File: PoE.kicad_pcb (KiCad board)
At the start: 4 copper layers, 102.5 x 35 mm, 88 parts, among them J1001 8P8C_LED_Shielded_x2, J1002 8P8C_LED_Shielded_x2, Q2001 FDC86244, U1001 7490220122, U1002 TCMT1107, U2001 TPS23751PWP, U2002 TCMT1107, U2003 TLV431ACDBZR

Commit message: New layout attempt
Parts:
- CR2001: moved to B.Cu
- D1001, D1002, D1006, D1007: moved to F.Cu
- moved C1006 36.8 mm to (70.5, 48.2), turned to 0 degrees
- moved C2002 14.4 mm to (51.6, 45.2), turned to 180 degrees
- moved D1006 12.9 mm to (48.4, 39.0)
- moved D1001 12.8 mm to (57.4, 39.0)
- moved U1002 9.84 mm to (95.2, 25.1)
- moved CR2001 9.65 mm to (56.5, 26.0)
- moved U2002 9.22 mm to (95.2, 28.8)
- moved R2001 6.30 mm to (58.5, 25.0)
- moved R2003 6.30 mm to (54.5, 25.0)
- moved R2002 6.10 mm to (58.5, 27.0)
- moved R2004 6.00 mm to (54.5, 27.0)
- moved C2009 5.90 mm to (67.6, 44.0)
- moved D1008 4.64 mm to (48.4, 32.0)
- moved D1003 4.46 mm to (57.4, 32.0)
- moved D1009 3.11 mm to (48.4, 39.0)
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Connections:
- U2001 pad V: (no net) -> VSS
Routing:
- net T2P: track 0.00 -> 54.0 mm, vias 0 -> 2
- net /Flyback/T_PRI: track 0.00 -> 48.6 mm, vias 0 -> 7
- net /D_IN: track 26.1 -> 69.9 mm, vias 8 -> 7
- net Net-(U2001-SRT): track 2.01 -> 34.8 mm, vias 0 -> 2
- net VSS: track 0.00 -> 26.4 mm, vias 0 -> 2
- net Net-(U2001-CS): track 0.00 -> 24.7 mm, vias 0 -> 2
- net /C_IN: track 32.4 -> 56.4 mm, vias 7 -> 6
- net /VSS_PRIME: track 17.9 -> 41.2 mm, vias 8 -> 3
- net /VDD_PRIME: track 17.9 -> 40.2 mm, vias 0 -> 3
- net Net-(U2001-VB): track 12.8 -> 32.8 mm, vias 0 -> 1
- net /Flyback/VC: track 0.00 -> 17.7 mm, vias 0 -> 2
- net VDD: track 3.23 -> 19.7 mm, vias 1 -> 2
- net /B_IN: track 35.5 -> 48.6 mm, vias 11 -> 7
- net Net-(U2001-CTL): track 5.27 -> 11.8 mm, vias 0 -> 1
- net Net-(U2001-GATE): track 0.00 -> 5.59 mm, vias 0 -> 1
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- removed copper zone on In2.Cu, net /A_IN
- removed copper zone on In1.Cu, net /B_IN
- removed copper zone on In2.Cu, net /B_IN
- removed copper zone on In2.Cu, net /C_IN
- removed copper zone on In1.Cu, net /D_IN
- removed copper zone on F.Cu, net /VDD_PRIME
- removed copper zone on B.Cu, net /VSS_PRIME
- removed copper zone on F.Cu, net /VSS_PRIME

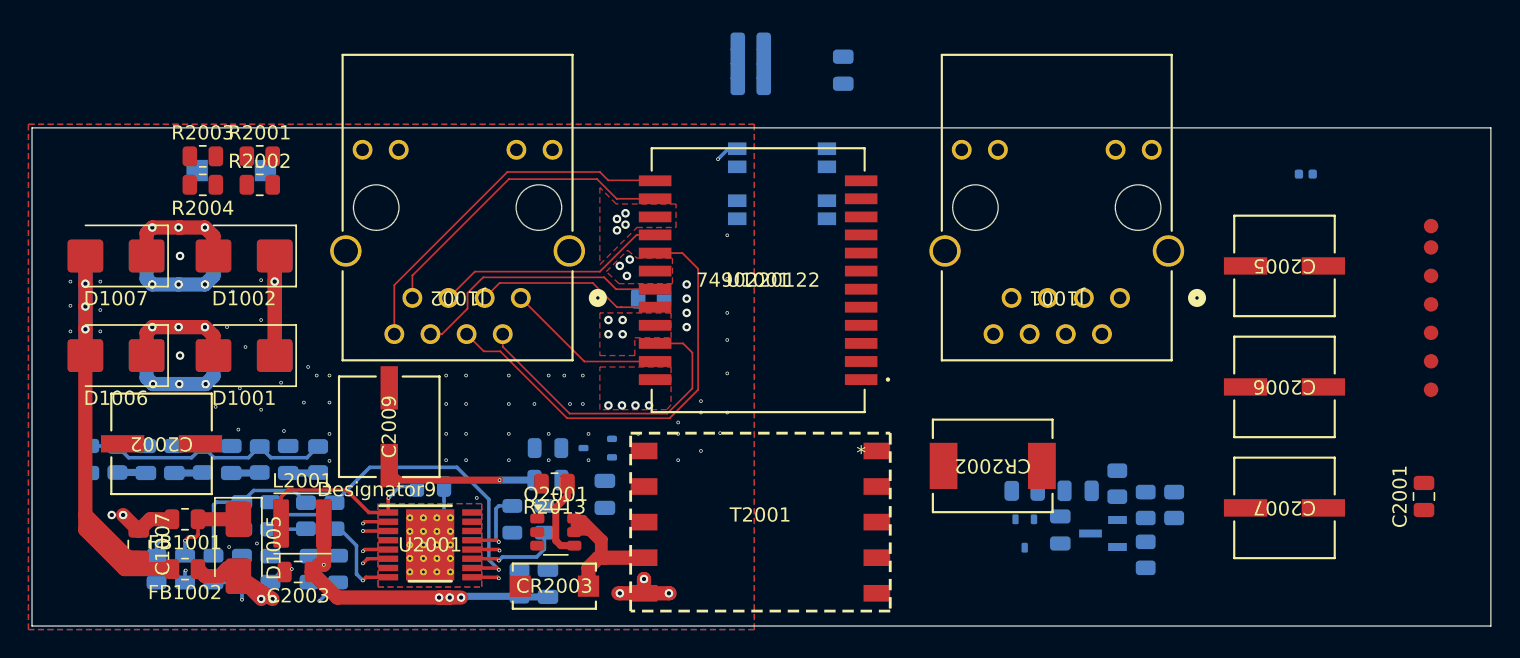
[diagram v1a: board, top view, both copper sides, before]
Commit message: Changed main FET
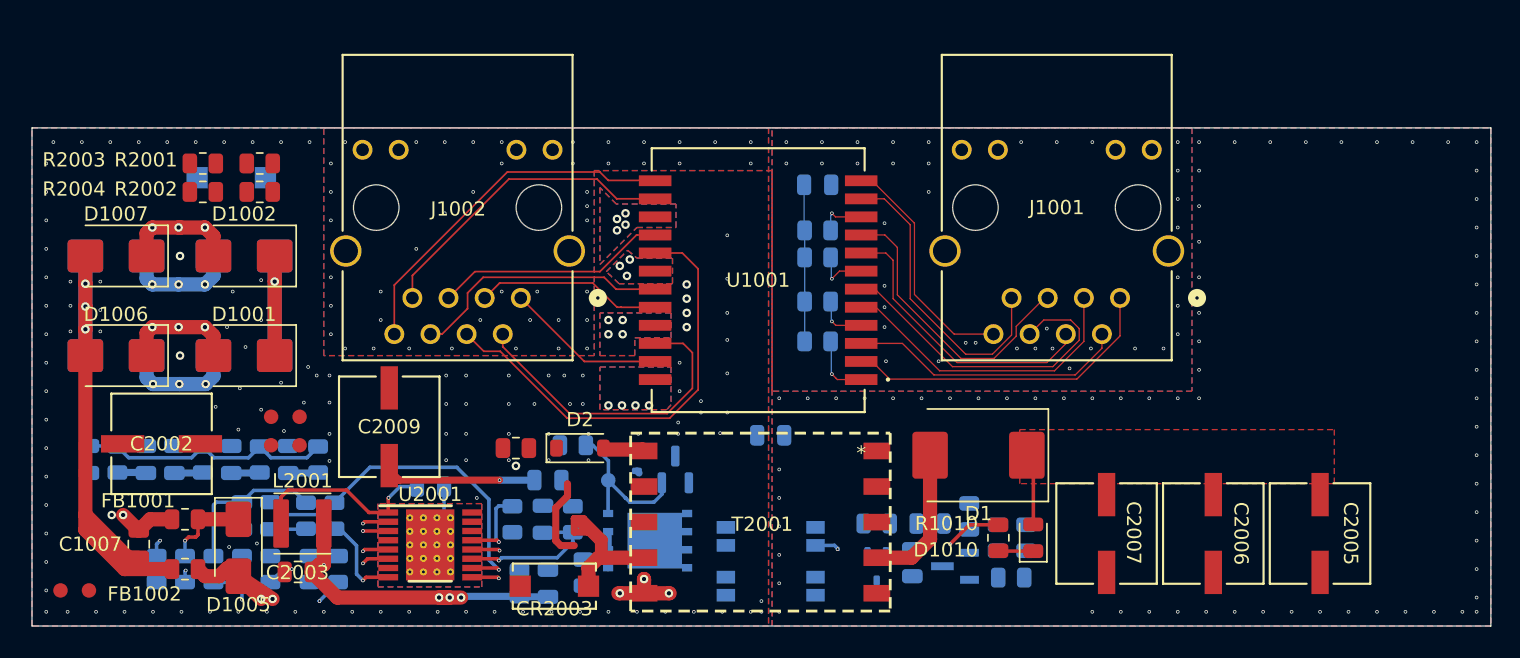
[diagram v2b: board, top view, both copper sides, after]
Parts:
- removed CR2002: MBRS540T3G, footprints:DIODE_SMC_7P15X6P25_ONS
- removed D2001: BAS16W, Package_TO_SOT_SMD:SOT-323_SC-70
- removed Q2001: FDC86244, Package_TO_SOT_SMD:SuperSOT-6
- removed TP1007: TestPoint, SparkFun-Connector:TestPoint-1.0mm
- added D1: B340, Diode_SMD:D_SMC, F.Cu at (109.0, 46.0)
- added D2: 1N4148W, Diode_SMD:D_SOD-123, F.Cu at (81.0, 45.5)
- added D3: BAS16W, Package_TO_SOT_SMD:SOT-323_SC-70, B.Cu at (84.0, 47.8)
- added Q1: SI7898DP-T1-E3, footprints:MOSFET_50DP-T1-E3_VIS, B.Cu at (85.8, 52.0)
- added Q2: MMBT3906, Package_TO_SOT_SMD:SOT-23, B.Cu at (87.7, 47.0)
- added R1: 10k, Resistor_SMD:R_0805_2012Metric, B.Cu at (80.5, 45.3)
- C2001, R2013: moved to B.Cu
- D1010: footprint LED_SMD:LED_0402_1005Metric -> LED_SMD:LED_0805_2012Metric; moved to F.Cu
- R1010: moved to F.Cu
- R2006, R2007, R2009, R2012: footprint LED_SMD:LED_0805_2012Metric -> Resistor_SMD:R_0805_2012Metric
- R2008: value 49.9 -> 10; footprint LED_SMD:LED_0805_2012Metric -> Resistor_SMD:R_0805_2012Metric; moved to F.Cu
- R2010: value 49.9 -> 43.2; footprint LED_SMD:LED_0805_2012Metric -> Resistor_SMD:R_0805_2012Metric
- R2011: value 0 -> 332; footprint LED_SMD:LED_0805_2012Metric -> Resistor_SMD:R_0805_2012Metric
- moved TP1006 99.3 mm to (44.5, 55.5), turned to 0 degrees
- moved TP1001 97.7 mm to (46.5, 55.5), turned to 0 degrees
- moved TP1005 82.1 mm to (59.3, 43.3), turned to 0 degrees
- moved TP1003 81.9 mm to (59.3, 45.3), turned to 0 degrees
- moved TP1002 80.1 mm to (61.3, 45.3), turned to 0 degrees
- moved TP1004 79.5 mm to (61.3, 43.3), turned to 0 degrees
- moved C2001 46.1 mm to (94.4, 44.6), turned to 0 degrees
- moved D1010 31.9 mm to (112.8, 51.8), turned to 90 degrees
- moved R1010 29.6 mm to (110.4, 51.8), turned to 90 degrees
- moved U1002 26.6 mm to (94.4, 51.7)
- moved U2002 26.5 mm to (94.4, 55.2)
- moved R1001 21.5 mm to (97.7, 38.0)
- moved C2005 19.0 mm to (133.0, 51.5), turned to -90 degrees
- moved R1002 17.8 mm to (97.7, 35.2)
- moved R1003 13.9 mm to (97.7, 32.1)
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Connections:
- net Net-(C1002-Pad2) renamed /TEST_A
- net Net-(C1003-Pad2) renamed /TEST_B
- net Net-(C1004-Pad2) renamed /TEST_C
- net Net-(C1005-Pad2) renamed /TEST_D
- C1001 pad 2: unconnected-(C1001-Pad2) -> GNDPWR
- J1001 pad SH: GNDREF -> GNDPWR
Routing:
- net (no net): track 0.00 -> 67.7 mm, vias 0 -> 8
- net Net-(U2001-SRT): track 34.8 -> 0.00 mm, vias 2 -> 0
- net /ETH3: track 0.00 -> 23.3 mm
- net /ETH0: track 0.00 -> 22.6 mm
- net /ETH2: track 0.00 -> 21.4 mm
- net /ETH6: track 0.00 -> 21.3 mm
- net /ETH5: track 0.00 -> 20.8 mm
- net /ETH1: track 0.00 -> 20.6 mm
- net /ETH4: track 0.00 -> 20.4 mm
- net /ETH7: track 0.00 -> 16.7 mm
- net Net-(U2001-CS): track 24.7 -> 10.5 mm, vias 2 -> 1
- net Net-(R1010-Pad2): track 0.00 -> 13.8 mm, vias 0 -> 1
- net Net-(D3-K): track 0.00 -> 11.2 mm
- net Net-(C1001-Pad1): track 0.00 -> 11.1 mm
- net Net-(D1-A): track 0.00 -> 10.2 mm
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- added copper zone on F.Cu, net +5V
- added copper zone on B.Cu, net /A_IN
- added copper zone on In1.Cu, net /A_IN
- added copper zone on In2.Cu, net /A_IN
- added copper zone on B.Cu, net /B_IN
- added copper zone on In1.Cu, net /B_IN
- added copper zone on In2.Cu, net /B_IN
- added copper zone on B.Cu, net /C_IN
- added copper zone on In1.Cu, net /C_IN
- added copper zone on In2.Cu, net /C_IN
- added copper zone on B.Cu, net /D_IN
- added copper zone on In1.Cu, net /D_IN
- added copper zone on In2.Cu, net /D_IN
- added copper zone on B.Cu, net GNDPWR
- added copper zone on F.Cu, net GNDPWR
- added copper zone on In1.Cu, net GNDPWR
- added copper zone on In2.Cu, net GNDPWR
- added copper zone on B.Cu, net GNDREF
- added copper zone on F.Cu, net GNDREF
- added copper zone on In1.Cu, net GNDREF
- added copper zone on In2.Cu, net GNDREF

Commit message: More routing
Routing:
- net T2P: track 52.4 -> 30.8 mm, vias 1 -> 2
- net /B_IN: track 48.6 -> 66.4 mm, vias 7 -> 8
- net /C_IN: track 56.4 -> 71.8 mm
- net /A_IN: track 43.3 -> 54.5 mm
- net /D_IN: track 69.9 -> 75.8 mm
- net GND: vias 124 -> 113

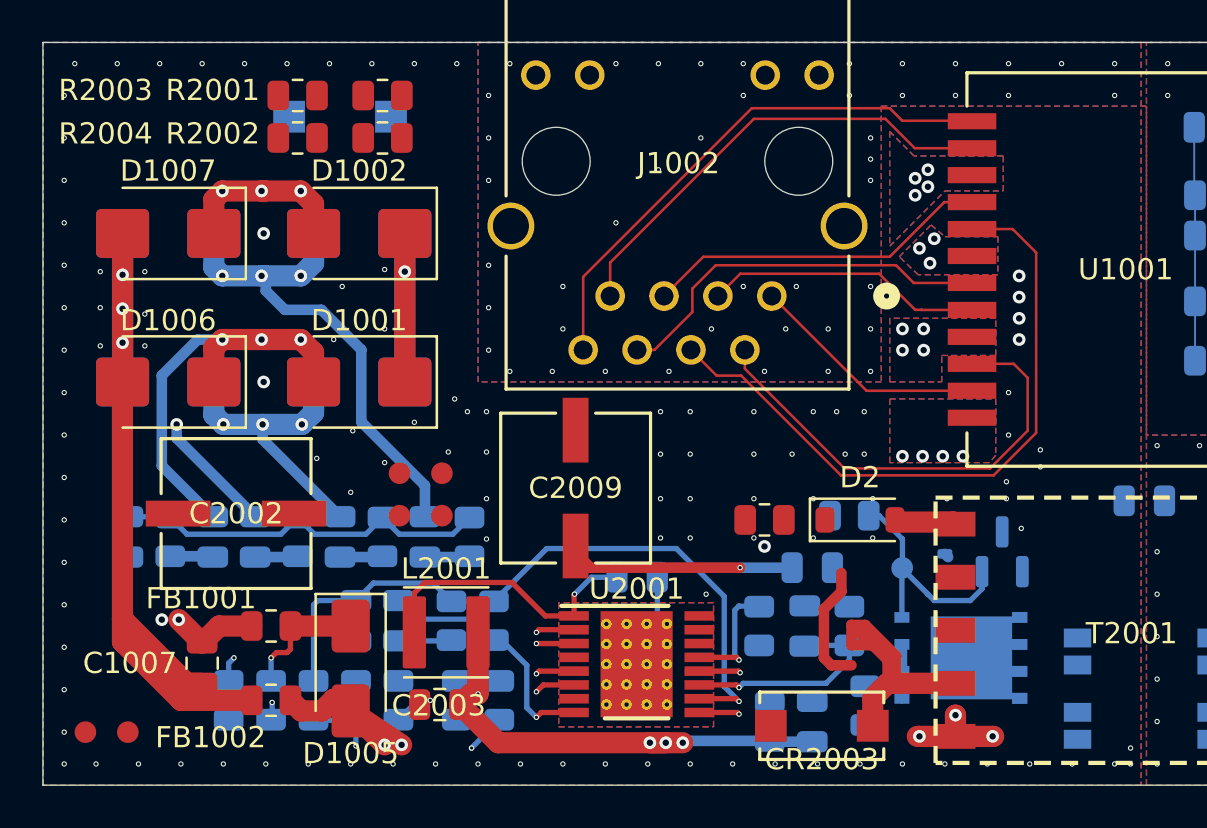
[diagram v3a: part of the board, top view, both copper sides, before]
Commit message: Added more routing
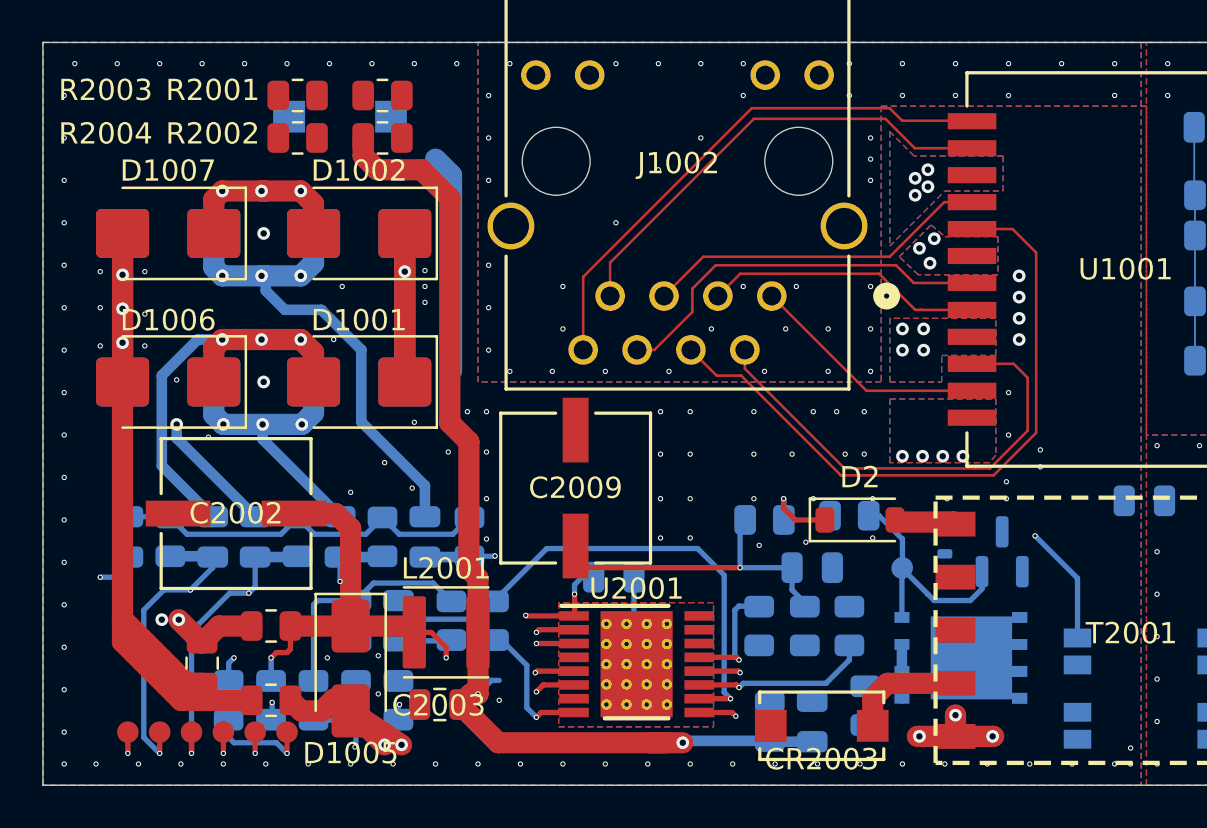
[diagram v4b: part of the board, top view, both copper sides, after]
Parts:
- removed C2010: 330p, Capacitor_SMD:C_0805_2012Metric
- removed R2007: 750k, Resistor_SMD:R_0805_2012Metric
- R2008: moved to B.Cu
- moved TP1004 17.0 mm to (49.5, 55.5)
- moved R1009 16.8 mm to (78.4, 50.5)
- moved TP1005 16.6 mm to (48.0, 55.5)
- moved TP1002 13.5 mm to (52.5, 55.5)
- moved TP1003 13.2 mm to (51.0, 55.5)
- moved TP1006 9.50 mm to (54.0, 55.5)
- moved C1006 1.10 mm to (69.4, 48.2)
- turned R2008 to 180 degrees
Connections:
- C2008 pad 1: /Flyback/VC -> VC
- C2009 pad 1: /Flyback/VC -> VC
- R2008 pad 2: /Flyback/VC -> VC
- U2001 pad 12: /Flyback/VC -> VC
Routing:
- net (no net): track 67.7 -> 0.00 mm, vias 8 -> 2
- net /Flyback/T_PRI: track 48.6 -> 85.7 mm, vias 7 -> 5
- net Net-(U2001-SRT): track 0.00 -> 35.4 mm, vias 0 -> 2
- net GNDPWR: track 0.00 -> 31.7 mm, vias 82 -> 83
- net /TEST_C: track 2.12 -> 25.9 mm, vias 0 -> 2
- net VC: track 0.00 -> 22.7 mm, vias 0 -> 2
- net VDD: track 19.7 -> 38.5 mm, vias 2 -> 5
- net /Flyback/VC: track 17.7 -> 0.00 mm, vias 2 -> 0
- net /TEST_A: track 2.02 -> 14.7 mm, vias 0 -> 2
- net /TEST_D: track 2.02 -> 14.2 mm, vias 0 -> 2
- net /TEST_B: track 2.02 -> 14.0 mm, vias 0 -> 2
- net Net-(U2001-RT): track 0.00 -> 9.59 mm, vias 0 -> 2
- net Net-(CR2003-Pad2): track 14.9 -> 5.49 mm
- net VSS: track 26.4 -> 35.6 mm, vias 2 -> 3
- net Net-(Q1-S-Pad1): track 10.1 -> 4.33 mm
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
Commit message: Finished routing now needs review
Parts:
- removed Q1: SI7898DP-T1-E3, footprints:MOSFET_50DP-T1-E3_VIS
- added Q2001: SI7898DP-T1-E3, footprints:MOSFET_50DP-T1-E3_VIS, B.Cu at (85.8, 52.0)
- moved CR2003 4.50 mm to (79.2, 50.7)
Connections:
- net Net-(D1-A) renamed /Flyback/5V_PRI
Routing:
- net Net-(U2001-CTL): track 11.8 -> 75.9 mm, vias 1 -> 3
- net Net-(U2002-A): track 0.00 -> 25.1 mm
- net Net-(U1002-A): track 0.00 -> 19.2 mm, vias 0 -> 2
- net Net-(D2002-A): track 0.00 -> 19.1 mm
- net Net-(D3-A): track 0.00 -> 16.9 mm, vias 0 -> 3
- net Net-(D2-A): track 2.79 -> 17.5 mm, vias 0 -> 4
- net Net-(D2002-K): track 0.00 -> 10.4 mm
- net /Flyback/5V_PRI: track 10.2 -> 0.00 mm
- net Net-(C2004-Pad2): track 0.00 -> 10.00 mm, vias 0 -> 1
- net Net-(U2003-REF): track 0.00 -> 8.28 mm
- net +5V: track 8.00 -> 13.0 mm
- net Net-(Q2001-PadS): track 4.33 -> 7.92 mm
- net Net-(C2012-Pad1): track 0.00 -> 1.89 mm
- net Net-(D3-K): track 11.2 -> 10.6 mm
- net Net-(R1010-Pad2): track 13.8 -> 14.2 mm, vias 1 -> 2
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- added copper zone on F.Cu, net /Flyback/5V_PRI

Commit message: Added buck
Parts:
- added C1: 10u, Capacitor_SMD:C_0805_2012Metric, B.Cu at (128.9, 25.7)
- added C10: 4.7u, Capacitor_SMD:C_0805_2012Metric, B.Cu at (133.4, 37.8)
- added C2: 100n, Capacitor_SMD:C_0805_2012Metric, B.Cu at (128.9, 28.7)
- added C3: 10u, Capacitor_SMD:C_0805_2012Metric, B.Cu at (128.9, 31.8)
- added C4: 100n, Capacitor_SMD:C_0805_2012Metric, B.Cu at (128.9, 34.8)
- added C5: 100n, Capacitor_SMD:C_0805_2012Metric, B.Cu at (128.9, 37.8)
- added C6: 10u, Capacitor_SMD:C_0805_2012Metric, B.Cu at (133.4, 25.7)
- added C7: 10u, Capacitor_SMD:C_0805_2012Metric, B.Cu at (133.4, 28.7)
- added C8: 10u, Capacitor_SMD:C_0805_2012Metric, B.Cu at (133.4, 31.8)
- added C9: 10u, Capacitor_SMD:C_0805_2012Metric, B.Cu at (133.4, 34.8)
- added J1: Conn_01x03, SparkFun-Connector:1x03, F.Cu at (137.3, 25.7)
- added L1: 4.7u, Inductor_SMD:L_Abracon_ASPI-4030S, F.Cu at (130.6, 30.3)
- added R2: 10k, Resistor_SMD:R_0805_2012Metric, B.Cu at (137.8, 25.7)
- added R3: 7.5k, Resistor_SMD:R_0805_2012Metric, B.Cu at (137.8, 28.6)
- added R3004: TC33X-2-203E, Potentiometer_SMD:Potentiometer_Bourns_TC33X_Vertical, F.Cu at (139.4, 32.8)
- added R4: 100k, Resistor_SMD:R_0805_2012Metric, B.Cu at (137.8, 31.6)
- added U1: TPS563203, Package_TO_SOT_SMD:SOT-563, F.Cu at (130.5, 26.5)
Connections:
- net +5V renamed +12V
